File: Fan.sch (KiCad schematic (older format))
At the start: 11 parts, among them Q2 DMN65D8L-7, Q3 AOD476, Q4 AOD476, U11 OPA4170, U8 MCP4801

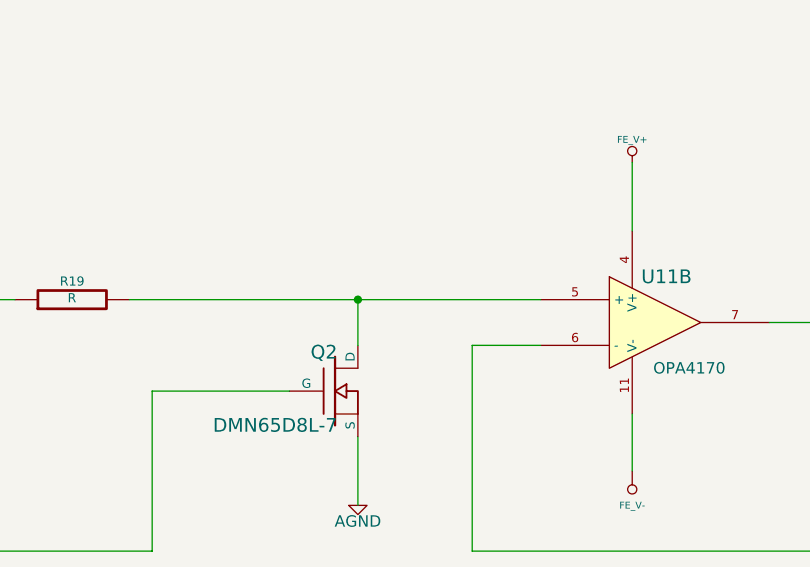
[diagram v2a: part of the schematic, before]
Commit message: Test points added, silk screen updates
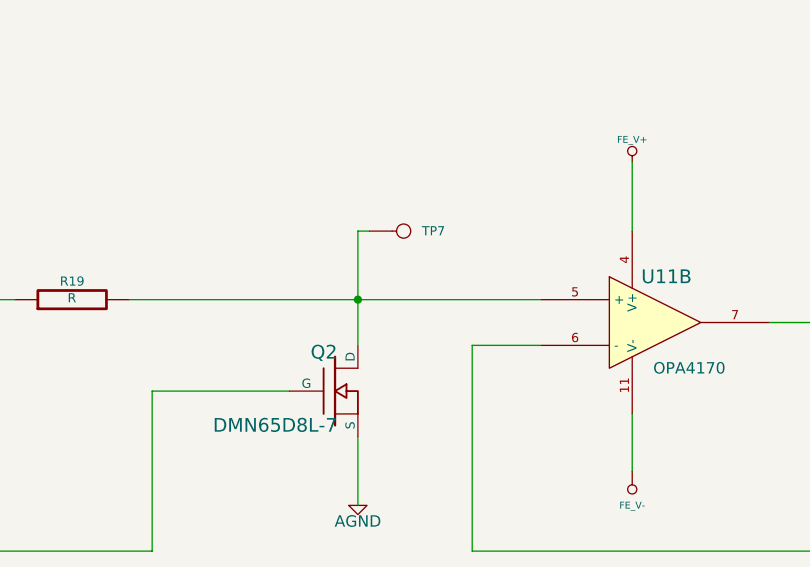
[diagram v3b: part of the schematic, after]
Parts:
- added TP7: DAC_OUT, symbol CONN_1
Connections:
- wire segments 47 -> 48
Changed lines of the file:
@@
 	10500 6100 1500 6100
 Wire Wire Line
-	4600 2700 4600 2500
+	4600 2200 4600 2700
 Connection ~ 4600 2500
 Wire Wire Line
@@
 	1500 5000 6400 5000
 $Comp
-L +12C #PWR50
+L +12C #PWR039
 U 1 1 52FBEABF
 P 7200 700
-F 0 "#PWR50" H 7200 670 30  0001 C CNN
+F 0 "#PWR039" H 7200 670 30  0001 C CNN
 F 1 "+12C" H 7200 810 40  0000 C CNN
 F 2 "" H 7200 700 60  0000 C CNN
@@
 	1000 2800 1200 2800
 $Comp
-L +5V #PWR45
+L +5V #PWR040
 U 1 1 530AC1D4
 P 1900 1350
-F 0 "#PWR45" H 1900 1440 20  0001 C CNN
+F 0 "#PWR040" H 1900 1440 20  0001 C CNN
 F 1 "+5V" H 1900 1440 30  0000 C CNN
 F 2 "" H 1900 1350 60  0000 C CNN
@@
 $EndComp
 $Comp
-L AGND #PWR44
+L AGND #PWR041
 U 1 1 530AC1E0
 P 1400 1600
-F 0 "#PWR44" H 1400 1600 40  0001 C CNN
+F 0 "#PWR041" H 1400 1600 40  0001 C CNN
 F 1 "AGND" H 1400 1530 50  0000 C CNN
 F 2 "" H 1400 1600 60  0000 C CNN
@@
 $EndComp
 $Comp
-L FE_V+ #PWR48
+L FE_V+ #PWR042
 U 1 1 530BD846
 P 5800 1900
-F 0 "#PWR48" H 5800 2000 30  0001 C CNN
+F 0 "#PWR042" H 5800 2000 30  0001 C CNN
 F 1 "FE_V+" H 5800 2000 30  0000 C CNN
 F 2 "" H 5800 1900 60  0000 C CNN
@@
 $EndComp
 $Comp
-L AGND #PWR46
+L AGND #PWR043
 U 1 1 53162F09
 P 1900 3450
-F 0 "#PWR46" H 1900 3450 40  0001 C CNN
+F 0 "#PWR043" H 1900 3450 40  0001 C CNN
 F 1 "AGND" H 1900 3380 50  0000 C CNN
 F 2 "" H 1900 3450 60  0000 C CNN
@@
 $EndComp
 $Comp
-L AGND #PWR47
+L AGND #PWR044
 U 1 1 53162F25
 P 4600 3400
-F 0 "#PWR47" H 4600 3400 40  0001 C CNN
+F 0 "#PWR044" H 4600 3400 40  0001 C CNN
 F 1 "AGND" H 4600 3330 50  0000 C CNN
 F 2 "" H 4600 3400 60  0000 C CNN
@@
 $EndComp
 $Comp
-L AGND #PWR51
+L AGND #PWR045
 U 1 1 53162F3A
 P 7200 5700
-F 0 "#PWR51" H 7200 5700 40  0001 C CNN
+F 0 "#PWR045" H 7200 5700 40  0001 C CNN
 F 1 "AGND" H 7200 5630 50  0000 C CNN
 F 2 "" H 7200 5700 60  0000 C CNN
@@
 $EndComp
 $Comp
-L AGND #PWR52
+L AGND #PWR046
 U 1 1 53162F4F
 P 7750 850
-F 0 "#PWR52" H 7750 850 40  0001 C CNN
+F 0 "#PWR046" H 7750 850 40  0001 C CNN
 F 1 "AGND" H 7750 780 50  0000 C CNN
 F 2 "" H 7750 850 60  0000 C CNN
@@
 	1    0    0    -1
 $EndComp
+$Comp
+L CONN_1 TP7
+U 1 1 5322467E
+P 4800 2200
+F 0 "TP7" H 4880 2200 40  0000 L CNN
+F 1 "DAC_OUT" H 4800 2255 30  0001 C CNN
+F 2 "" H 4800 2200 60  0000 C CNN
+F 3 "" H 4800 2200 60  0000 C CNN
+	1    4800 2200
+	1    0    0    -1
+$EndComp
+Wire Wire Line
+	4600 2200 4650 2200
 $EndSCHEMATC

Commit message: Added some R/C to analog sections
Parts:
- added C32, C33: C, symbol C
- added R59, R60, R61: 0, symbol R
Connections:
- wire segments 48 -> 55
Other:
- moved on the sheet: Q2, TP7, U11B
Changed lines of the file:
@@
 L LM324 U11
 U 2 1 52F026D6
-P 5900 2600
-F 0 "U11" H 5950 2800 60  0000 C CNN
-F 1 "OPA4170" H 6050 2400 50  0000 C CNN
-F 2 "" H 5900 2600 60  0000 C CNN
-F 3 "" H 5900 2600 60  0000 C CNN
-	2    5900 2600
+P 5500 2600
+F 0 "U11" H 5550 2800 60  0000 C CNN
+F 1 "OPA4170" H 5650 2400 50  0000 C CNN
+F 2 "" H 5500 2600 60  0000 C CNN
+F 3 "" H 5500 2600 60  0000 C CNN
+	2    5500 2600
 	1    0    0    -1
 $EndComp
@@
 $EndComp
 Wire Wire Line
-	7200 3600 5100 3600
-Wire Wire Line
 	7200 5300 7200 5700
 Wire Wire Line
-	6400 2600 6900 2600
-Wire Wire Line
-	5800 1900 5800 2200
-Wire Wire Line
-	5800 3250 5800 3000
-Wire Wire Line
-	5100 3600 5100 2700
-Wire Wire Line
-	5100 2700 5400 2700
+	5400 1900 5400 2200
+Wire Wire Line
+	5400 3250 5400 3000
+Wire Wire Line
+	4700 3600 4700 2700
+Wire Wire Line
+	4700 2700 5000 2700
 Connection ~ 7200 3600
 Wire Wire Line
-	3600 2500 5400 2500
-Wire Wire Line
-	4600 3400 4600 3100
+	3600 2500 5000 2500
+Wire Wire Line
+	4200 3950 4200 3750
 Wire Wire Line
 	7200 4400 1500 4400
@@
 	2900 2500 3100 2500
 Wire Wire Line
-	7200 800  7200 700
+	7200 700  7200 800
 Wire Wire Line
 	7200 1700 10500 1700
@@
 	7200 1900 7200 2400
 Wire Wire Line
-	7200 2100 7000 2100
+	6700 2100 7200 2100
 Wire Wire Line
 	7000 2100 7000 2000
@@
 	7000 1600 7000 1500
 Wire Wire Line
-	7000 1500 7200 1500
+	6700 1500 7200 1500
 Connection ~ 7200 1500
 Connection ~ 7200 4400
@@
 	10500 6100 1500 6100
 Wire Wire Line
-	4600 2200 4600 2700
-Connection ~ 4600 2500
-Wire Wire Line
-	1500 3600 3700 3600
-Wire Wire Line
-	3700 3600 3700 2900
-Wire Wire Line
-	3700 2900 4300 2900
+	4200 2200 4200 2700
+Connection ~ 4200 2500
+Wire Wire Line
+	1500 3600 3350 3600
+Wire Wire Line
+	3350 3600 3350 2900
+Wire Wire Line
+	3350 2900 3900 2900
 Text HLabel 1500 5000 0    60   Input ~ 0
 FAN_MODE
@@
 L MOSFET_N_NUM Q2
 U 1 1 53091E18
-P 4500 2900
-F 0 "Q2" H 4510 3070 60  0000 R CNN
-F 1 "DMN65D8L-7" H 4510 2750 60  0000 R CNN
-F 2 "" H 4500 2900 60  0000 C CNN
-F 3 "" H 4500 2900 60  0000 C CNN
-F 4 "Diodes Inc" H 4500 2900 60  0001 C CNN "MFG Name"
-F 5 "DMN65D8L-7" H 4500 2900 60  0001 C CNN "MFG Part Number"
-	1    4500 2900
+P 4100 2900
+F 0 "Q2" H 4110 3070 60  0000 R CNN
+F 1 "DMN65D8L-7" H 4110 2750 60  0000 R CNN
+F 2 "" H 4100 2900 60  0000 C CNN
+F 3 "" H 4100 2900 60  0000 C CNN
+F 4 "Diodes Inc" H 4100 2900 60  0001 C CNN "MFG Name"
+F 5 "DMN65D8L-7" H 4100 2900 60  0001 C CNN "MFG Part Number"
+	1    4100 2900
 	1    0    0    -1
 $EndComp
@@
 L FE_V- #PWR49
 U 1 1 530BD840
-P 5800 3250
-F 0 "#PWR49" H 5800 3450 40  0001 C CNN
-F 1 "FE_V-" H 5800 3400 30  0000 C CNN
-F 2 "" H 5800 3250 60  0000 C CNN
-F 3 "" H 5800 3250 60  0000 C CNN
-	1    5800 3250
+P 5400 3250
+F 0 "#PWR49" H 5400 3450 40  0001 C CNN
+F 1 "FE_V-" H 5400 3400 30  0000 C CNN
+F 2 "" H 5400 3250 60  0000 C CNN
+F 3 "" H 5400 3250 60  0000 C CNN
+	1    5400 3250
 	-1   0    0    1
 $EndComp
@@
 L FE_V+ #PWR042
 U 1 1 530BD846
-P 5800 1900
-F 0 "#PWR042" H 5800 2000 30  0001 C CNN
-F 1 "FE_V+" H 5800 2000 30  0000 C CNN
-F 2 "" H 5800 1900 60  0000 C CNN
-F 3 "" H 5800 1900 60  0000 C CNN
-	1    5800 1900
+P 5400 1900
+F 0 "#PWR042" H 5400 2000 30  0001 C CNN
+F 1 "FE_V+" H 5400 2000 30  0000 C CNN
+F 2 "" H 5400 1900 60  0000 C CNN
+F 3 "" H 5400 1900 60  0000 C CNN
+	1    5400 1900
 	1    0    0    -1
 $EndComp
@@
 L AGND #PWR044
 U 1 1 53162F25
-P 4600 3400
-F 0 "#PWR044" H 4600 3400 40  0001 C CNN
-F 1 "AGND" H 4600 3330 50  0000 C CNN
-F 2 "" H 4600 3400 60  0000 C CNN
-F 3 "" H 4600 3400 60  0000 C CNN
-	1    4600 3400
+P 4200 3950
+F 0 "#PWR044" H 4200 3950 40  0001 C CNN
+F 1 "AGND" H 4200 3880 50  0000 C CNN
+F 2 "" H 4200 3950 60  0000 C CNN
+F 3 "" H 4200 3950 60  0000 C CNN
+	1    4200 3950
 	1    0    0    -1
 $EndComp
@@
 L CONN_1 TP7
 U 1 1 5322467E
-P 4800 2200
-F 0 "TP7" H 4880 2200 40  0000 L CNN
-F 1 "DAC_OUT" H 4800 2255 30  0001 C CNN
-F 2 "" H 4800 2200 60  0000 C CNN
-F 3 "" H 4800 2200 60  0000 C CNN
-	1    4800 2200
-	1    0    0    -1
-$EndComp
-Wire Wire Line
-	4600 2200 4650 2200
+P 4400 2200
+F 0 "TP7" H 4480 2200 40  0000 L CNN
+F 1 "DAC_OUT" H 4400 2255 30  0001 C CNN
+F 2 "" H 4400 2200 60  0000 C CNN
+F 3 "" H 4400 2200 60  0000 C CNN
+	1    4400 2200
+	1    0    0    -1
+$EndComp
+Wire Wire Line
+	4200 2200 4250 2200
+$Comp
+L R R60
+U 1 1 532392DE
+P 6450 2600
+F 0 "R60" V 6530 2600 40  0000 C CNN
+F 1 "0" V 6457 2601 40  0000 C CNN
+F 2 "" V 6380 2600 30  0000 C CNN
+F 3 "" H 6450 2600 30  0000 C CNN
+	1    6450 2600
+	0    -1   -1   0
+$EndComp
+Wire Wire Line
+	6000 2600 6200 2600
+Wire Wire Line
+	6700 2600 6900 2600
+$Comp
+L C C32
+U 1 1 5323937C
+P 6100 3050
+F 0 "C32" H 6100 3150 40  0000 L CNN
+F 1 "C" H 6106 2965 40  0000 L CNN
+F 2 "" H 6138 2900 30  0000 C CNN
+F 3 "" H 6100 3050 60  0000 C CNN
+	1    6100 3050
+	1    0    0    -1
+$EndComp
+Wire Wire Line
+	6100 2850 6100 2600
+Connection ~ 6100 2600
+Wire Wire Line
+	6100 3250 6100 3600
+Connection ~ 6100 3600
+$Comp
+L R R61
+U 1 1 53239408
+P 6650 3600
+F 0 "R61" V 6730 3600 40  0000 C CNN
+F 1 "0" V 6657 3601 40  0000 C CNN
+F 2 "" V 6580 3600 30  0000 C CNN
+F 3 "" H 6650 3600 30  0000 C CNN
+	1    6650 3600
+	0    -1   -1   0
+$EndComp
+Wire Wire Line
+	7200 3600 6900 3600
+Wire Wire Line
+	4700 3600 6400 3600
+$Comp
+L C C33
+U 1 1 532394D3
+P 6700 1800
+F 0 "C33" H 6700 1900 40  0000 L CNN
+F 1 "C" H 6706 1715 40  0000 L CNN
+F 2 "" H 6738 1650 30  0000 C CNN
+F 3 "" H 6700 1800 60  0000 C CNN
+	1    6700 1800
+	1    0    0    -1
+$EndComp
+Wire Wire Line
+	6700 2100 6700 2000
+Connection ~ 7000 2100
+Wire Wire Line
+	6700 1600 6700 1500
+Connection ~ 7000 1500
+$Comp
+L R R59
+U 1 1 53239565
+P 4200 3500
+F 0 "R59" V 4280 3500 40  0000 C CNN
+F 1 "0" V 4207 3501 40  0000 C CNN
+F 2 "" V 4130 3500 30  0000 C CNN
+F 3 "" H 4200 3500 30  0000 C CNN
+	1    4200 3500
+	1    0    0    -1
+$EndComp
+Wire Wire Line
+	4200 3250 4200 3100
 $EndSCHEMATC

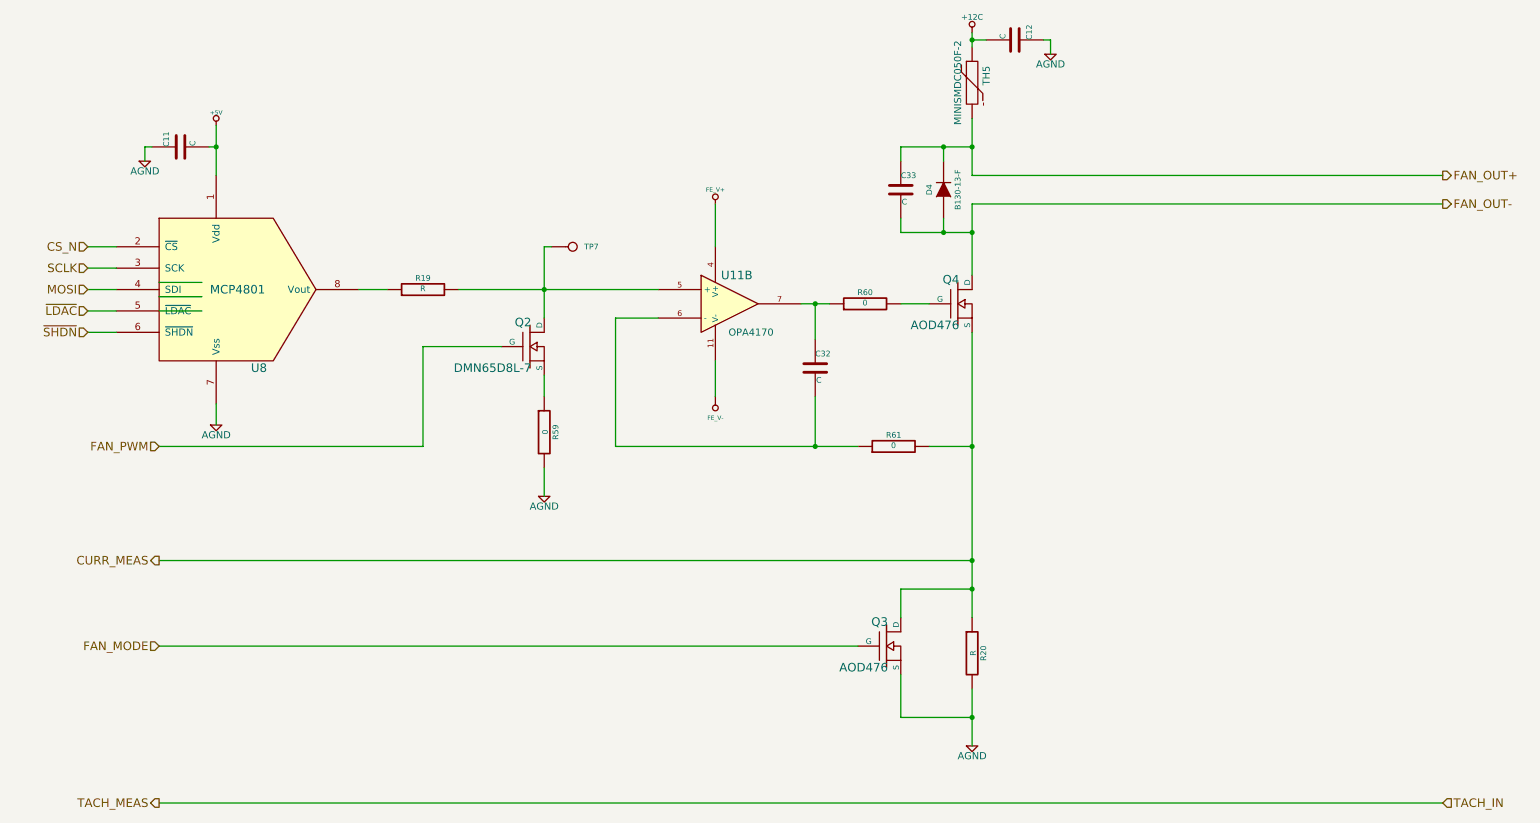
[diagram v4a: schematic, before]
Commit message: Assigned values to passives in fan and thermocouple schematics
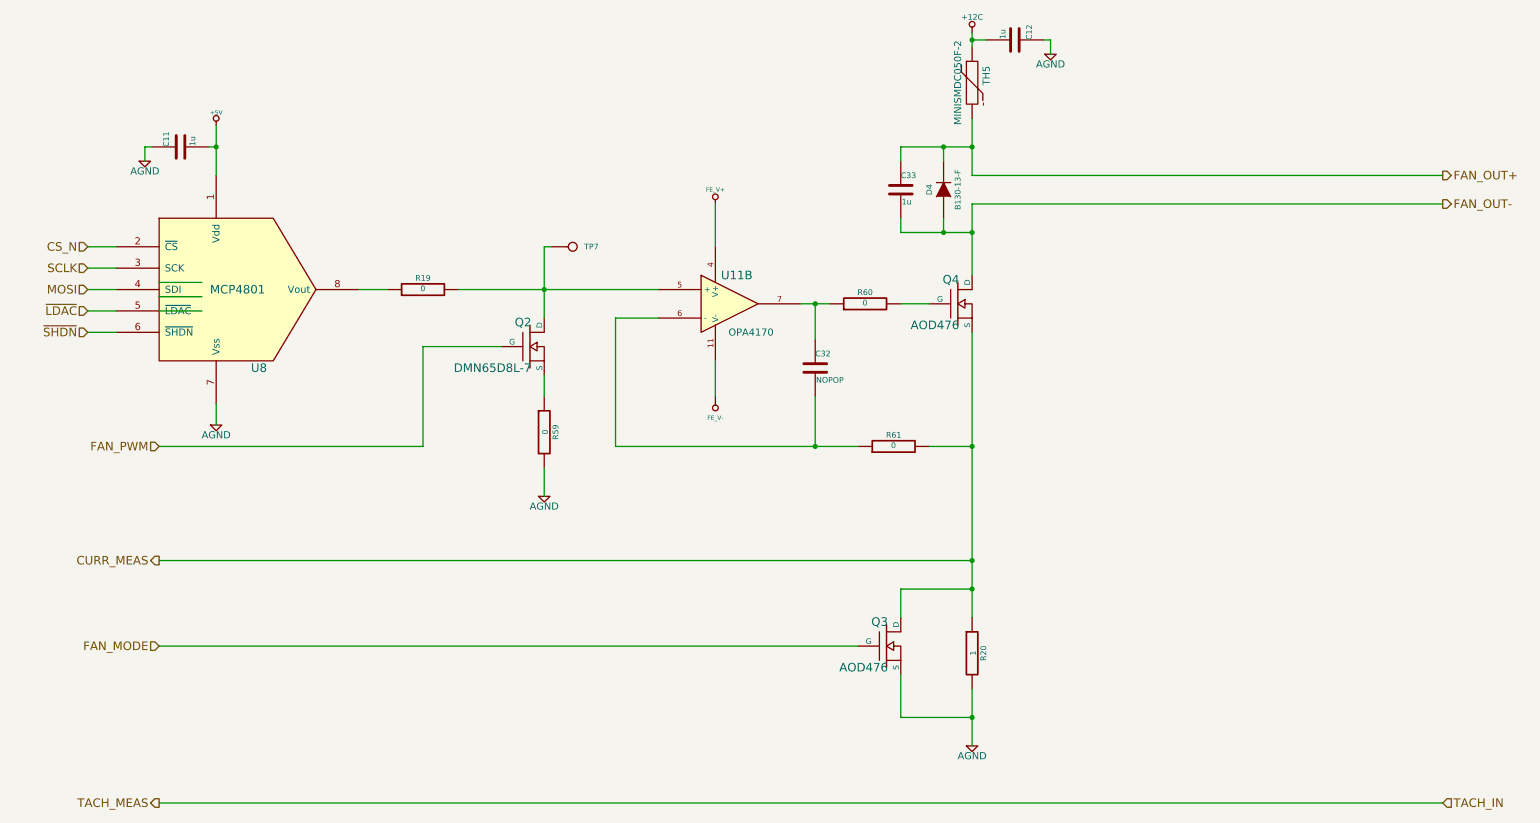
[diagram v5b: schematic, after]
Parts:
- C11, C12, C33: value C -> 1u
- C32: value C -> NOPOP
- R19: value R -> 0
- R20: value R -> 1
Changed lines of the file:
@@
 P 7200 5050
 F 0 "R20" V 7280 5050 40  0000 C CNN
-F 1 "R" V 7207 5051 40  0000 C CNN
+F 1 "1" V 7207 5051 40  0000 C CNN
 F 2 "" V 7130 5050 30  0000 C CNN
 F 3 "" H 7200 5050 30  0000 C CNN
@@
 P 3350 2500
 F 0 "R19" V 3430 2500 40  0000 C CNN
-F 1 "R" V 3357 2501 40  0000 C CNN
+F 1 "0" V 3357 2501 40  0000 C CNN
 F 2 "" V 3280 2500 30  0000 C CNN
 F 3 "" H 3350 2500 30  0000 C CNN
@@
 P 1650 1500
 F 0 "C11" H 1650 1600 40  0000 L CNN
-F 1 "C" H 1656 1415 40  0000 L CNN
+F 1 "1u" H 1656 1415 40  0000 L CNN
 F 2 "" H 1688 1350 30  0000 C CNN
 F 3 "" H 1650 1500 60  0000 C CNN
@@
 P 7500 750
 F 0 "C12" H 7500 850 40  0000 L CNN
-F 1 "C" H 7506 665 40  0000 L CNN
+F 1 "1u" H 7506 665 40  0000 L CNN
 F 2 "" H 7538 600 30  0000 C CNN
 F 3 "" H 7500 750 60  0000 C CNN
@@
 P 6100 3050
 F 0 "C32" H 6100 3150 40  0000 L CNN
-F 1 "C" H 6106 2965 40  0000 L CNN
+F 1 "NOPOP" H 6106 2965 40  0000 L CNN
 F 2 "" H 6138 2900 30  0000 C CNN
 F 3 "" H 6100 3050 60  0000 C CNN
@@
 P 6700 1800
 F 0 "C33" H 6700 1900 40  0000 L CNN
-F 1 "C" H 6706 1715 40  0000 L CNN
+F 1 "1u" H 6706 1715 40  0000 L CNN
 F 2 "" H 6738 1650 30  0000 C CNN
 F 3 "" H 6700 1800 60  0000 C CNN

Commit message: Back-annotated footprints into the schematic
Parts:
- C11, C12, C32, C33: footprint (none) -> Capacitors_SMD:c_0805
- D4: footprint (none) -> Diodes_SMD:Diode-SMA_Standard
- Q2: footprint (none) -> SMD_Packages:SOT23EBC
- Q3, Q4: footprint (none) -> SMD_Packages:DPAK2
- R19, R59, R60, R61: footprint (none) -> SMD_Packages:SM0805
- R20: footprint (none) -> SMD_Packages:SM1206
- TH5: footprint (none) -> SMD_Packages:SM1812
- TP7: footprint (none) -> BenchBudEE:TestPointTH
- U11: footprint (none) -> SMD_Packages:SO14E
- U8: footprint (none) -> SMD_Packages:SO8N
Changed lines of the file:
@@
 F 0 "U11" H 5550 2800 60  0000 C CNN
 F 1 "OPA4170" H 5650 2400 50  0000 C CNN
-F 2 "" H 5500 2600 60  0000 C CNN
+F 2 "SMD_Packages:SO14E" H 5500 2600 60  0001 C CNN
 F 3 "" H 5500 2600 60  0000 C CNN
 	2    5500 2600
@@
 F 0 "R20" V 7280 5050 40  0000 C CNN
 F 1 "1" V 7207 5051 40  0000 C CNN
-F 2 "" V 7130 5050 30  0000 C CNN
+F 2 "SMD_Packages:SM1206" V 7130 5050 30  0001 C CNN
 F 3 "" H 7200 5050 30  0000 C CNN
 	1    7200 5050
@@
 F 0 "R19" V 3430 2500 40  0000 C CNN
 F 1 "0" V 3357 2501 40  0000 C CNN
-F 2 "" V 3280 2500 30  0000 C CNN
+F 2 "SMD_Packages:SM0805" V 3280 2500 30  0001 C CNN
 F 3 "" H 3350 2500 30  0000 C CNN
 	1    3350 2500
@@
 F 0 "TH5" V 7300 1100 50  0000 C CNN
 F 1 "MINISMDC050F-2" V 7100 1050 50  0000 C CNN
-F 2 "" H 7200 1050 60  0000 C CNN
+F 2 "SMD_Packages:SM1812" H 7200 1050 60  0001 C CNN
 F 3 "" H 7200 1050 60  0000 C CNN
 F 4 "TE Connectivity" H 7200 1050 60  0001 C CNN "MFG Name"
@@
 F 0 "D4" H 7000 1900 40  0000 C CNN
 F 1 "B130-13-F" H 7000 1700 40  0000 C CNN
-F 2 "" H 7000 1800 60  0000 C CNN
+F 2 "Diodes_SMD:Diode-SMA_Standard" H 7000 1800 60  0001 C CNN
 F 3 "" H 7000 1800 60  0000 C CNN
 F 4 "Diodes Inc" H 7000 1800 60  0001 C CNN "MFG Name"
@@
 F 0 "U8" H 2200 1950 60  0000 C CNN
 F 1 "MCP4801" H 2050 2500 60  0000 C CNN
-F 2 "" H 1900 2500 60  0000 C CNN
+F 2 "SMD_Packages:SO8N" H 1900 2500 60  0001 C CNN
 F 3 "" H 1900 2500 60  0000 C CNN
 	1    1900 2500
@@
 F 0 "C11" H 1650 1600 40  0000 L CNN
 F 1 "1u" H 1656 1415 40  0000 L CNN
-F 2 "" H 1688 1350 30  0000 C CNN
+F 2 "Capacitors_SMD:c_0805" H 1688 1350 30  0001 C CNN
 F 3 "" H 1650 1500 60  0000 C CNN
 	1    1650 1500
@@
 F 0 "C12" H 7500 850 40  0000 L CNN
 F 1 "1u" H 7506 665 40  0000 L CNN
-F 2 "" H 7538 600 30  0000 C CNN
+F 2 "Capacitors_SMD:c_0805" H 7538 600 30  0001 C CNN
 F 3 "" H 7500 750 60  0000 C CNN
 	1    7500 750
@@
 F 0 "Q4" H 7110 2770 60  0000 R CNN
 F 1 "AOD476" H 7110 2450 60  0000 R CNN
-F 2 "" H 7100 2600 60  0000 C CNN
+F 2 "SMD_Packages:DPAK2" H 7100 2600 60  0001 C CNN
 F 3 "" H 7100 2600 60  0000 C CNN
 F 4 "Alpha and Omega" H 7100 2600 60  0001 C CNN "MFG Name"
@@
 F 0 "Q3" H 6610 5170 60  0000 R CNN
 F 1 "AOD476" H 6610 4850 60  0000 R CNN
-F 2 "" H 6600 5000 60  0000 C CNN
+F 2 "SMD_Packages:DPAK2" H 6600 5000 60  0001 C CNN
 F 3 "" H 6600 5000 60  0000 C CNN
 F 4 "Alpha and Omega" H 6600 5000 60  0001 C CNN "MFG Name"
@@
 F 0 "Q2" H 4110 3070 60  0000 R CNN
 F 1 "DMN65D8L-7" H 4110 2750 60  0000 R CNN
-F 2 "" H 4100 2900 60  0000 C CNN
+F 2 "SMD_Packages:SOT23EBC" H 4100 2900 60  0001 C CNN
 F 3 "" H 4100 2900 60  0000 C CNN
 F 4 "Diodes Inc" H 4100 2900 60  0001 C CNN "MFG Name"
@@
 F 0 "TP7" H 4480 2200 40  0000 L CNN
 F 1 "DAC_OUT" H 4400 2255 30  0001 C CNN
-F 2 "" H 4400 2200 60  0000 C CNN
+F 2 "BenchBudEE:TestPointTH" H 4400 2200 60  0001 C CNN
 F 3 "" H 4400 2200 60  0000 C CNN
 	1    4400 2200
@@
 F 0 "R60" V 6530 2600 40  0000 C CNN
 F 1 "0" V 6457 2601 40  0000 C CNN
-F 2 "" V 6380 2600 30  0000 C CNN
+F 2 "SMD_Packages:SM0805" V 6380 2600 30  0001 C CNN
 F 3 "" H 6450 2600 30  0000 C CNN
 	1    6450 2600
@@
 F 0 "C32" H 6100 3150 40  0000 L CNN
 F 1 "NOPOP" H 6106 2965 40  0000 L CNN
-F 2 "" H 6138 2900 30  0000 C CNN
+F 2 "Capacitors_SMD:c_0805" H 6138 2900 30  0001 C CNN
 F 3 "" H 6100 3050 60  0000 C CNN
 	1    6100 3050
@@
 F 0 "R61" V 6730 3600 40  0000 C CNN
 F 1 "0" V 6657 3601 40  0000 C CNN
-F 2 "" V 6580 3600 30  0000 C CNN
+F 2 "SMD_Packages:SM0805" V 6580 3600 30  0001 C CNN
 F 3 "" H 6650 3600 30  0000 C CNN
 	1    6650 3600
@@
 F 0 "C33" H 6700 1900 40  0000 L CNN
 F 1 "1u" H 6706 1715 40  0000 L CNN
-F 2 "" H 6738 1650 30  0000 C CNN
+F 2 "Capacitors_SMD:c_0805" H 6738 1650 30  0001 C CNN
 F 3 "" H 6700 1800 60  0000 C CNN
 	1    6700 1800
@@
 F 0 "R59" V 4280 3500 40  0000 C CNN
 F 1 "0" V 4207 3501 40  0000 C CNN
-F 2 "" V 4130 3500 30  0000 C CNN
+F 2 "SMD_Packages:SM0805" V 4130 3500 30  0001 C CNN
 F 3 "" H 4200 3500 30  0000 C CNN
 	1    4200 3500
